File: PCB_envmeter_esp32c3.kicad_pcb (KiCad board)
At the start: 2 copper layers, 72 x 47.5 mm, 31 parts, among them J1 USB_C_Receptacle_USB2.0_16P, J3 AE-BME680, J4 SSD1306, Q1 2SC2001, SW1 Reset, SW2 Mode, U1 ESP32-C3-WROOM-02, U2 AP7333-33SAG, U3 NJM2845DL1-33, U4 OSRB38C9AA

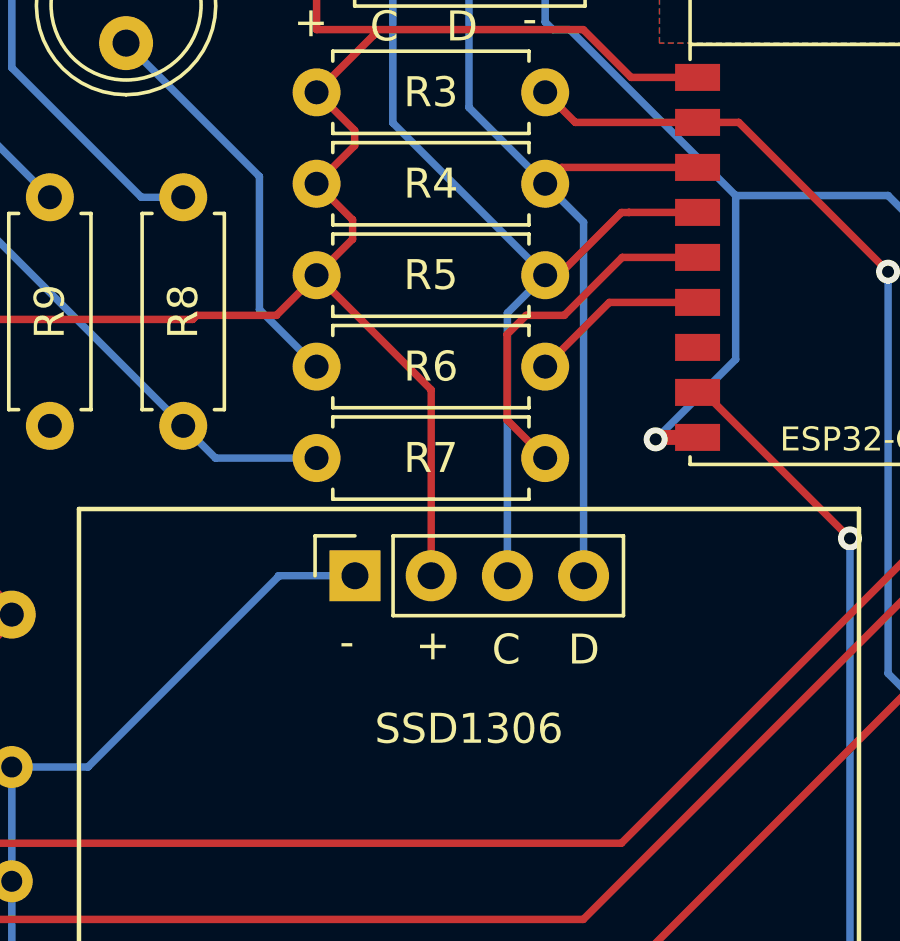
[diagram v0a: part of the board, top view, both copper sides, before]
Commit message: Adjust OLED position
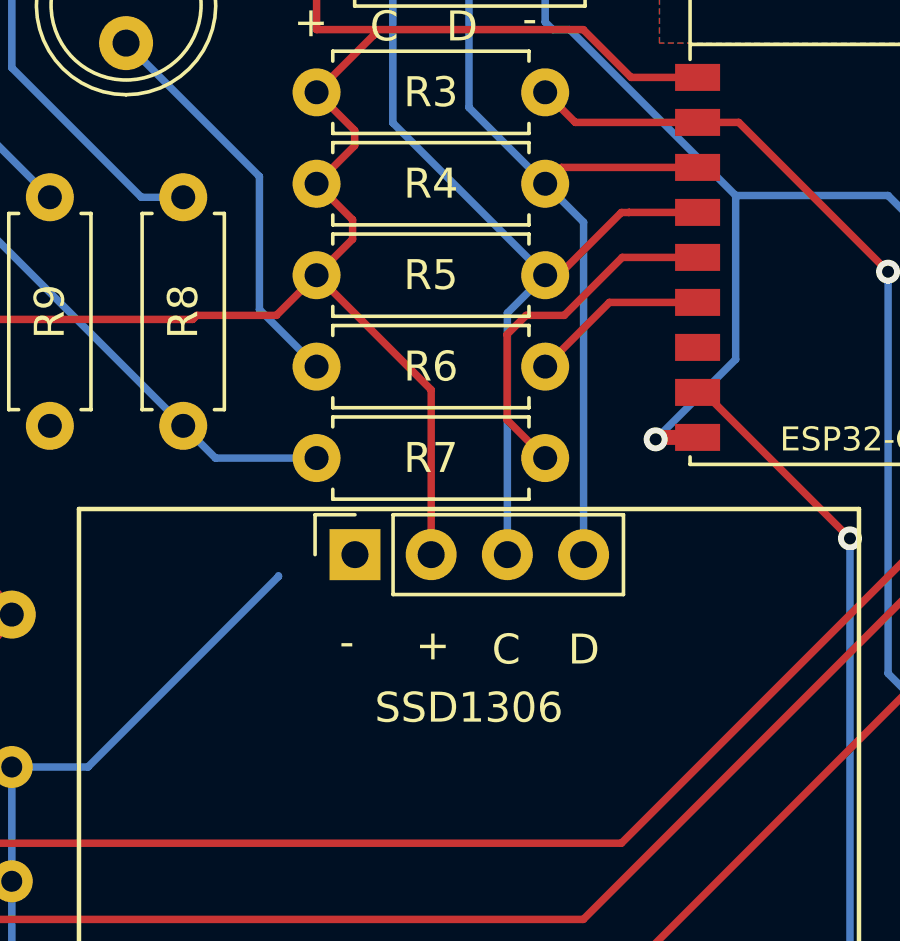
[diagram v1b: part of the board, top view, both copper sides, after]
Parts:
- moved J4 0.70 mm to (68.6, 57.7)
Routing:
- net GND: track 197.3 -> 194.7 mm
- net SDA: track 27.2 -> 26.5 mm
- net SCL: track 29.1 -> 28.4 mm
- net +3.3V: track 66.2 -> 65.5 mm
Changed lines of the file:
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@@
   )
   (footprint "Connector_PinSocket_2.54mm:PinSocket_1x04_P2.54mm_Vertical" (layer "F.Cu")
-    (at 68.59 58.395 90)
+    (at 68.59 57.691 90)
     (descr "Through hole straight socket strip, 1x04, 2.54mm pitch, single row (from Kicad 4.0.7), script generated")
     (tags "Through hole socket strip THT 1x04 2.54mm single row")
@@
   (segment (start 100.295 70.035) (end 100.33 70.035) (width 0.25) (layer "B.Cu") (net 2))
   (segment (start 50.8 69.85) (end 50.165 69.215) (width 0.25) (layer "B.Cu") (net 2))
-  (segment (start 66.04 58.395) (end 68.59 58.395) (width 0.25) (layer "B.Cu") (net 2))
   (segment (start 43.18 47.81) (end 43.18 44.254) (width 0.25) (layer "B.Cu") (net 2))
   (segment (start 57.15 64.77) (end 59.69 64.77) (width 0.25) (layer "B.Cu") (net 2))
@@
   (segment (start 74.93 38.075) (end 74.93 39.936) (width 0.25) (layer "B.Cu") (net 2))
   (segment (start 77.793 41.783) (end 76.2 40.19) (width 0.25) (layer "F.Cu") (net 3))
+  (segment (start 71.13 57.691) (end 71.13 52.196) (width 0.25) (layer "F.Cu") (net 3))
   (segment (start 68.58 43.55) (end 68.58 44.058) (width 0.25) (layer "F.Cu") (net 3))
   (segment (start 67.31 40.19) (end 67.31 38.075) (width 0.25) (layer "F.Cu") (net 3))
@@
   (segment (start 67.31 48.376) (end 65.971 49.715) (width 0.25) (layer "F.Cu") (net 3))
   (segment (start 67.31 42.28) (end 68.58 43.55) (width 0.25) (layer "F.Cu") (net 3))
-  (segment (start 71.13 52.196) (end 71.13 58.395) (width 0.25) (layer "F.Cu") (net 3))
   (segment (start 65.971 49.715) (end 63.315 49.715) (width 0.25) (layer "F.Cu") (net 3))
   (segment (start 49.21 48.26) (end 47.9675 47.0175) (width 0.25) (layer "F.Cu") (net 3))
@@
   (segment (start 69.85 43.296) (end 69.85 38.075) (width 0.25) (layer "B.Cu") (net 12))
   (segment (start 74.93 48.376) (end 69.85 43.296) (width 0.25) (layer "B.Cu") (net 12))
-  (segment (start 73.67 49.636) (end 73.67 58.395) (width 0.25) (layer "B.Cu") (net 12))
+  (segment (start 73.67 57.691) (end 73.67 49.636) (width 0.25) (layer "B.Cu") (net 12))
   (segment (start 75.475 44.783) (end 74.93 45.328) (width 0.25) (layer "F.Cu") (net 13))
   (segment (start 80.01 44.783) (end 75.475 44.783) (width 0.25) (layer "F.Cu") (net 13))
-  (segment (start 74.93 45.328) (end 76.21 46.608) (width 0.25) (layer "B.Cu") (net 13))
+  (segment (start 76.21 57.691) (end 76.21 46.608) (width 0.25) (layer "B.Cu") (net 13))
   (segment (start 74.93 45.328) (end 72.39 42.788) (width 0.25) (layer "B.Cu") (net 13))
   (segment (start 72.39 38.075) (end 72.39 42.788) (width 0.25) (layer "B.Cu") (net 13))
-  (segment (start 76.21 46.608) (end 76.21 58.395) (width 0.25) (layer "B.Cu") (net 13))
+  (segment (start 76.21 46.608) (end 74.93 45.328) (width 0.25) (layer "B.Cu") (net 13))
   (segment (start 77.071 49.283) (end 74.93 51.424) (width 0.25) (layer "F.Cu") (net 14))
   (segment (start 80.01 49.283) (end 77.071 49.283) (width 0.25) (layer "F.Cu") (net 14))
